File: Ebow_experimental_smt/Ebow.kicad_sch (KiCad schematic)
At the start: 9 parts, among them J1 Conn_01x02, U1 LM386

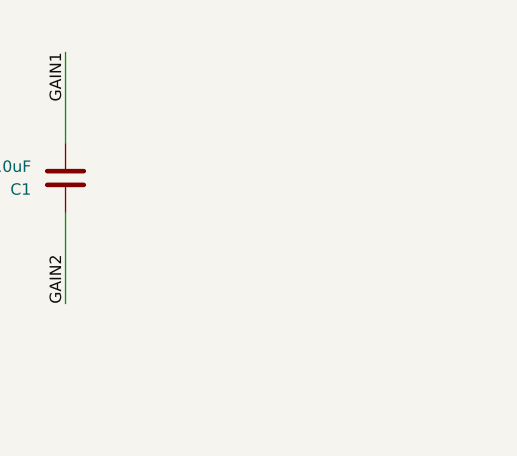
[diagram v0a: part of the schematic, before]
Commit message: Added smt version.
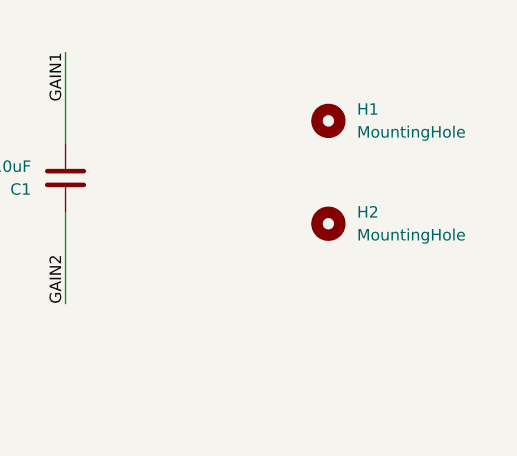
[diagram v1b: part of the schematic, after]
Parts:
- added H1, H2: MountingHole, MountingHole:MountingHole_2.5mm_Pad_TopBottom, symbol Mechanical:MountingHole
- C1, C2: footprint Capacitor_THT:CP_Radial_D5.0mm_P2.00mm -> Capacitor_SMD:C_Elec_4x5.8
- C3: footprint Capacitor_THT:C_Disc_D3.0mm_W2.0mm_P2.50mm -> Capacitor_SMD:C_0805_2012Metric_Pad1.18x1.45mm_HandSolder
- C4: footprint Capacitor_THT:CP_Radial_D8.0mm_P3.50mm -> Capacitor_SMD:CP_Elec_8x6.9
- L1, L2: footprint Buzzer_Beeper:Buzzer_D14mm_H7mm_P10mm -> Inductor_SMD:L_Taiyo-Yuden_NR-80xx_HandSoldering
- R1: footprint Resistor_THT:R_Axial_DIN0207_L6.3mm_D2.5mm_P15.24mm_Horizontal -> Resistor_SMD:R_0805_2012Metric_Pad1.20x1.40mm_HandSolder
- U1: footprint Package_DIP:DIP-8_W7.62mm_Socket -> Package_SO:SOIC-8_3.9x4.9mm_P1.27mm
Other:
- title: (none) -> Sustainer
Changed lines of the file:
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@@
 (kicad_sch (version 20211123) (generator eeschema)
   (paper "A4")
+  (title_block
+    (title "Sustainer")
+    (rev "A")
+  )
   (junction (at 127 145.415) (diameter 0) (color 0 0 0 0)
   )
@@
       (effects (font (size 1.27 1.27)) (justify right))
     )
-    (property "Footprint" "Capacitor_THT:C_Disc_D3.0mm_W2.0mm_P2.50mm" (id 2) (at 165.4048 127 0)
+    (property "Footprint" "Capacitor_SMD:C_0805_2012Metric_Pad1.18x1.45mm_HandSolder" (id 2) (at 165.4048 127 0)
       (effects (font (size 1.27 1.27)) hide)
     )
@@
       (effects (font (size 1.27 1.27)) (justify left))
     )
-    (property "Footprint" "Resistor_THT:R_Axial_DIN0207_L6.3mm_D2.5mm_P15.24mm_Horizontal" (id 2) (at 164.592 140.335 90)
+    (property "Footprint" "Resistor_SMD:R_0805_2012Metric_Pad1.20x1.40mm_HandSolder" (id 2) (at 164.592 140.335 90)
       (effects (font (size 1.27 1.27)) hide)
     )
@@
       (effects (font (size 1.27 1.27)) (justify left))
     )
-    (property "Footprint" "Buzzer_Beeper:Buzzer_D14mm_H7mm_P10mm" (id 2) (at 203.835 111.125 0)
-      (effects (font (size 1.27 1.27)) hide)
-    )
-    (property "Datasheet" "~" (id 3) (at 203.835 111.125 0)
+    (property "Footprint" "Inductor_SMD:L_Taiyo-Yuden_NR-80xx_HandSoldering" (id 2) (at 203.835 111.125 0)
+      (effects (font (size 1.27 1.27)) hide)
+    )
+    (property "Datasheet" "${KIPRJMOD}/datasheets/2108131830_SXN-Shun-Xiang-Nuo-Elec-SMNR6028-4R7MT_C266428.pdf" (id 3) (at 203.835 111.125 0)
       (effects (font (size 1.27 1.27)) hide)
     )
@@
       (effects (font (size 1.27 1.27)) (justify right))
     )
-    (property "Footprint" "Buzzer_Beeper:Buzzer_D14mm_H7mm_P10mm" (id 2) (at 89.535 108.585 0)
-      (effects (font (size 1.27 1.27)) hide)
-    )
-    (property "Datasheet" "~" (id 3) (at 89.535 108.585 0)
+    (property "Footprint" "Inductor_SMD:L_Taiyo-Yuden_NR-80xx_HandSoldering" (id 2) (at 89.535 108.585 0)
+      (effects (font (size 1.27 1.27)) hide)
+    )
+    (property "Datasheet" "${KIPRJMOD}/datasheets/2108131830_SXN-Shun-Xiang-Nuo-Elec-SMNR6028-4R7MT_C266428.pdf" (id 3) (at 89.535 108.585 0)
       (effects (font (size 1.27 1.27)) hide)
     )
@@
       (effects (font (size 1.27 1.27)) (justify right))
     )
-    (property "Footprint" "Capacitor_THT:CP_Radial_D5.0mm_P2.00mm" (id 2) (at 194.6402 35.56 0)
+    (property "Footprint" "Capacitor_SMD:C_Elec_4x5.8" (id 2) (at 194.6402 35.56 0)
       (effects (font (size 1.27 1.27)) hide)
     )
@@
       (effects (font (size 1.27 1.27)) (justify right))
     )
-    (property "Footprint" "Capacitor_THT:CP_Radial_D5.0mm_P2.00mm" (id 2) (at 163.4998 43.18 0)
+    (property "Footprint" "Capacitor_SMD:C_Elec_4x5.8" (id 2) (at 163.4998 43.18 0)
       (effects (font (size 1.27 1.27)) hide)
     )
@@
     (pin "1")
   )
+  (symbol (lib_id "Mechanical:MountingHole") (at 222.885 33.02 0) (unit 1)
+    (in_bom yes) (on_board yes) (fields_autoplaced)
+    (property "Reference" "H1" (id 0) (at 226.06 31.7499 0)
+      (effects (font (size 1.27 1.27)) (justify left))
+    )
+    (property "Value" "MountingHole" (id 1) (at 226.06 34.2899 0)
+      (effects (font (size 1.27 1.27)) (justify left))
+    )
+    (property "Footprint" "MountingHole:MountingHole_2.5mm_Pad_TopBottom" (id 2) (at 222.885 33.02 0)
+      (effects (font (size 1.27 1.27)) hide)
+    )
+    (property "Datasheet" "~" (id 3) (at 222.885 33.02 0)
+      (effects (font (size 1.27 1.27)) hide)
+    )
+  )
   (symbol (lib_id "power:+5V") (at 127 80.01 0) (unit 1)
     (in_bom yes) (on_board yes) (fields_autoplaced)
@@
     )
     (pin "1")
+  )
+  (symbol (lib_id "Mechanical:MountingHole") (at 222.885 44.45 0) (unit 1)
+    (in_bom yes) (on_board yes) (fields_autoplaced)
+    (property "Reference" "H2" (id 0) (at 226.06 43.1799 0)
+      (effects (font (size 1.27 1.27)) (justify left))
+    )
+    (property "Value" "MountingHole" (id 1) (at 226.06 45.7199 0)
+      (effects (font (size 1.27 1.27)) (justify left))
+    )
+    (property "Footprint" "MountingHole:MountingHole_2.5mm_Pad_TopBottom" (id 2) (at 222.885 44.45 0)
+      (effects (font (size 1.27 1.27)) hide)
+    )
+    (property "Datasheet" "~" (id 3) (at 222.885 44.45 0)
+      (effects (font (size 1.27 1.27)) hide)
+    )
   )
   (symbol (lib_id "Connector_Generic:Conn_01x02") (at 46.99 38.735 0) (mirror y) (unit 1)
@@
     (property "Reference" "C4" (id 0) (at 175.26 100.33 90))
     (property "Value" "220uF" (id 1) (at 175.26 102.87 90))
-    (property "Footprint" "Capacitor_THT:CP_Radial_D8.0mm_P3.50mm" (id 2) (at 179.07 106.3498 0)
+    (property "Footprint" "Capacitor_SMD:CP_Elec_8x6.9" (id 2) (at 179.07 106.3498 0)
       (effects (font (size 1.27 1.27)) hide)
     )
@@
     (property "Reference" "U1" (id 0) (at 139.7 102.616 0))
     (property "Value" "LM386" (id 1) (at 139.7 105.156 0))
-    (property "Footprint" "Package_DIP:DIP-8_W7.62mm_Socket" (id 2) (at 132.08 104.775 0)
-      (effects (font (size 1.27 1.27)) hide)
-    )
-    (property "Datasheet" "http://www.ti.com/lit/ds/symlink/lm386.pdf" (id 3) (at 134.62 102.235 0)
+    (property "Footprint" "Package_SO:SOIC-8_3.9x4.9mm_P1.27mm" (id 2) (at 132.08 104.775 0)
+      (effects (font (size 1.27 1.27)) hide)
+    )
+    (property "Datasheet" "${KIPRJMOD}/datasheets/lm386.pdf" (id 3) (at 134.62 102.235 0)
       (effects (font (size 1.27 1.27)) hide)
     )
@@
     )
     (path "/17c612b1-1712-43c4-bf42-da58958720f5"
-      (reference "C1") (unit 1) (value "10uF") (footprint "Capacitor_THT:CP_Radial_D5.0mm_P2.00mm")
+      (reference "C1") (unit 1) (value "10uF") (footprint "Capacitor_SMD:C_Elec_4x5.8")
     )
     (path "/1806c226-f868-413d-a730-b553d0b74cd3"
-      (reference "C2") (unit 1) (value "10uF") (footprint "Capacitor_THT:CP_Radial_D5.0mm_P2.00mm")
+      (reference "C2") (unit 1) (value "10uF") (footprint "Capacitor_SMD:C_Elec_4x5.8")
     )
     (path "/00fe35bc-98a8-4a57-8798-022f2f38780f"
-      (reference "C3") (unit 1) (value "47nF") (footprint "Capacitor_THT:C_Disc_D3.0mm_W2.0mm_P2.50mm")
+      (reference "C3") (unit 1) (value "47nF") (footprint "Capacitor_SMD:C_0805_2012Metric_Pad1.18x1.45mm_HandSolder")
     )
     (path "/95e2b8ef-b2ba-4938-97ca-cb0ef16712f6"
-      (reference "C4") (unit 1) (value "220uF") (footprint "Capacitor_THT:CP_Radial_D8.0mm_P3.50mm")
+      (reference "C4") (unit 1) (value "220uF") (footprint "Capacitor_SMD:CP_Elec_8x6.9")
+    )
+    (path "/310cf662-ee96-4e28-bf7a-f359466b8a24"
+      (reference "H1") (unit 1) (value "MountingHole") (footprint "MountingHole:MountingHole_2.5mm_Pad_TopBottom")
+    )
+    (path "/5ba09802-fc89-420d-9bc0-892b15911595"
+      (reference "H2") (unit 1) (value "MountingHole") (footprint "MountingHole:MountingHole_2.5mm_Pad_TopBottom")
     )
     (path "/86fa4628-2b3e-41e8-a65a-32e6da99fd1a"
@@
     )
     (path "/0fc6b024-f82b-4a82-bc84-87a221f28fe6"
-      (reference "L1") (unit 1) (value "L_Iron") (footprint "Buzzer_Beeper:Buzzer_D14mm_H7mm_P10mm")
+      (reference "L1") (unit 1) (value "L_Iron") (footprint "Inductor_SMD:L_Taiyo-Yuden_NR-80xx_HandSoldering")
     )
     (path "/0bff6920-0589-4a77-a48c-bd2c2345b946"
-      (reference "L2") (unit 1) (value "L_Iron") (footprint "Buzzer_Beeper:Buzzer_D14mm_H7mm_P10mm")
+      (reference "L2") (unit 1) (value "L_Iron") (footprint "Inductor_SMD:L_Taiyo-Yuden_NR-80xx_HandSoldering")
     )
     (path "/081ac558-1d49-471c-abf3-ed1a23f06285"
-      (reference "R1") (unit 1) (value "10R") (footprint "Resistor_THT:R_Axial_DIN0207_L6.3mm_D2.5mm_P15.24mm_Horizontal")
+      (reference "R1") (unit 1) (value "10R") (footprint "Resistor_SMD:R_0805_2012Metric_Pad1.20x1.40mm_HandSolder")
     )
     (path "/b3fe88ca-b472-4b17-9b69-956f1d81f7f1"
-      (reference "U1") (unit 1) (value "LM386") (footprint "Package_DIP:DIP-8_W7.62mm_Socket")
-    )
-  )
+      (reference "U1") (unit 1) (value "LM386") (footprint "Package_SO:SOIC-8_3.9x4.9mm_P1.27mm")
+    )
+  )

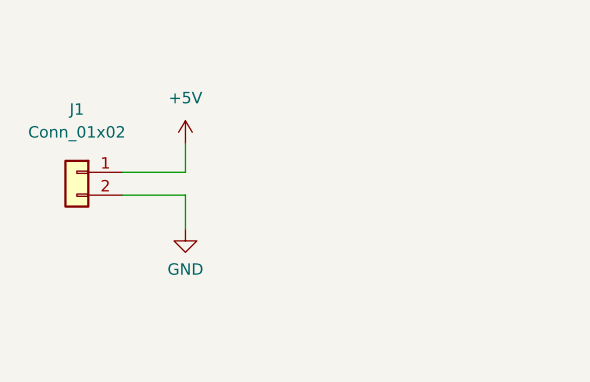
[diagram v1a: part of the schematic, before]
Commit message: updated schemas
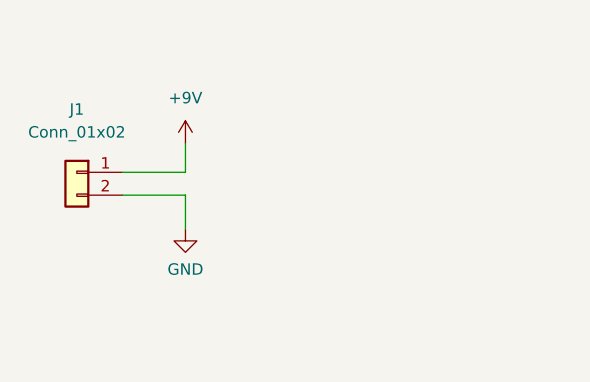
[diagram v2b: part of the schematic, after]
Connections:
- net +5V: no longer J1.1 (Pin_1)
- new net +9V: J1.1 (Pin_1)
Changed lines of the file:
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@@
     )
+  )
+  (symbol (lib_id "power:+9V") (at 59.055 35.56 0) (unit 1)
+    (in_bom yes) (on_board yes) (fields_autoplaced)
+    (property "Reference" "#PWR?" (id 0) (at 59.055 39.37 0)
+      (effects (font (size 1.27 1.27)) hide)
+    )
+    (property "Value" "+9V" (id 1) (at 59.055 30.48 0))
+    (property "Footprint" "" (id 2) (at 59.055 35.56 0)
+      (effects (font (size 1.27 1.27)) hide)
+    )
+    (property "Datasheet" "" (id 3) (at 59.055 35.56 0)
+      (effects (font (size 1.27 1.27)) hide)
+    )
+    (pin "1")
   )
   (symbol (lib_id "power:+5V") (at 127 80.01 0) (unit 1)
@@
     (pin "1")
   )
-  (symbol (lib_id "power:+5V") (at 59.055 35.56 0) (unit 1)
-    (in_bom yes) (on_board yes) (fields_autoplaced)
-    (property "Reference" "#PWR02" (id 0) (at 59.055 39.37 0)
-      (effects (font (size 1.27 1.27)) hide)
-    )
-    (property "Value" "+5V" (id 1) (at 59.055 30.48 0))
-    (property "Footprint" "" (id 2) (at 59.055 35.56 0)
-      (effects (font (size 1.27 1.27)) hide)
-    )
-    (property "Datasheet" "" (id 3) (at 59.055 35.56 0)
-      (effects (font (size 1.27 1.27)) hide)
-    )
-    (pin "1")
-  )
   (symbol (lib_id "Amplifier_Audio:LM386") (at 129.54 107.315 0) (unit 1)
     (in_bom yes) (on_board yes) (fields_autoplaced)
@@
       (reference "#PWR01") (unit 1) (value "GND") (footprint "")
     )
-    (path "/b14f207c-4c8e-4a7c-a74a-39cd24bc2d4c"
-      (reference "#PWR02") (unit 1) (value "+5V") (footprint "")
-    )
     (path "/92979cff-1e7c-4fc6-a0d2-82f65b7c20ae"
       (reference "#PWR03") (unit 1) (value "GND") (footprint "")
@@
       (reference "#PWR09") (unit 1) (value "GND") (footprint "")
     )
+    (path "/3e525ee9-d2a7-4d3c-a5be-81e97a45e5b0"
+      (reference "#PWR?") (unit 1) (value "+9V") (footprint "")
+    )
     (path "/17c612b1-1712-43c4-bf42-da58958720f5"

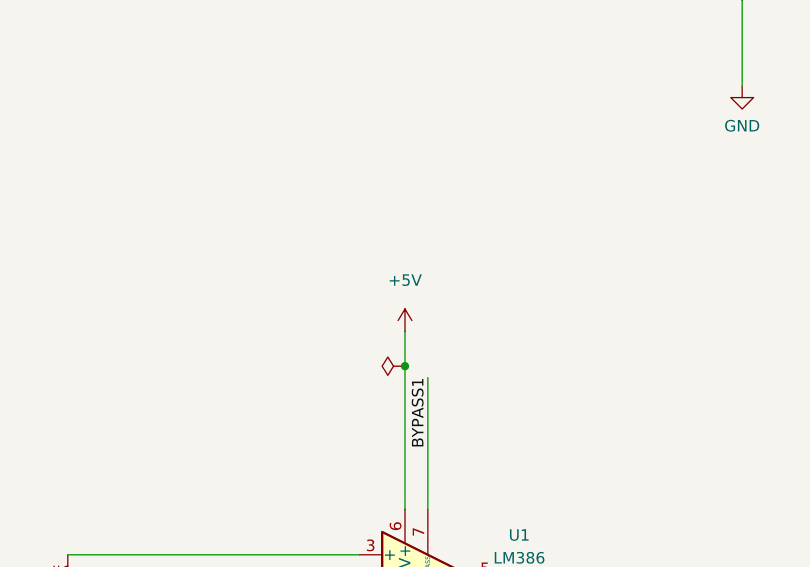
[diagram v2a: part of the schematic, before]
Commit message: updated power rail error
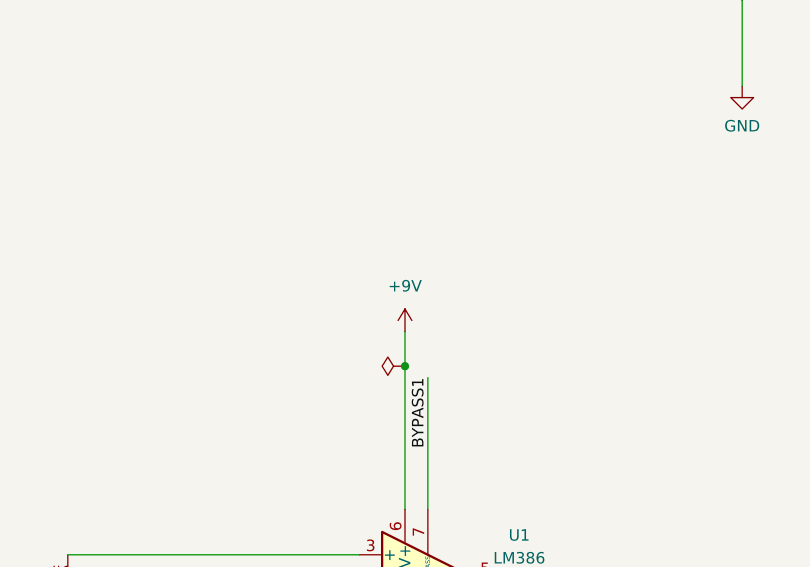
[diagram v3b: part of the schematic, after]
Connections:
- net +5V is gone; now on net +9V: U1.6 (V+)
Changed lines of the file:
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@@
     )
+  )
+  (symbol (lib_id "power:+9V") (at 127 80.01 0) (unit 1)
+    (in_bom yes) (on_board yes) (fields_autoplaced)
+    (property "Reference" "#PWR?" (id 0) (at 127 83.82 0)
+      (effects (font (size 1.27 1.27)) hide)
+    )
+    (property "Value" "+9V" (id 1) (at 127 74.93 0))
+    (property "Footprint" "" (id 2) (at 127 80.01 0)
+      (effects (font (size 1.27 1.27)) hide)
+    )
+    (property "Datasheet" "" (id 3) (at 127 80.01 0)
+      (effects (font (size 1.27 1.27)) hide)
+    )
+    (pin "1")
   )
   (symbol (lib_id "power:+9V") (at 59.055 35.56 0) (unit 1)
@@
     )
     (property "Datasheet" "" (id 3) (at 59.055 35.56 0)
-      (effects (font (size 1.27 1.27)) hide)
-    )
-    (pin "1")
-  )
-  (symbol (lib_id "power:+5V") (at 127 80.01 0) (unit 1)
-    (in_bom yes) (on_board yes) (fields_autoplaced)
-    (property "Reference" "#PWR04" (id 0) (at 127 83.82 0)
-      (effects (font (size 1.27 1.27)) hide)
-    )
-    (property "Value" "+5V" (id 1) (at 127 74.295 0))
-    (property "Footprint" "" (id 2) (at 127 80.01 0)
-      (effects (font (size 1.27 1.27)) hide)
-    )
-    (property "Datasheet" "" (id 3) (at 127 80.01 0)
       (effects (font (size 1.27 1.27)) hide)
     )
@@
       (reference "#PWR03") (unit 1) (value "GND") (footprint "")
     )
-    (path "/48b7a76d-e799-461e-8984-ba9b128240cc"
-      (reference "#PWR04") (unit 1) (value "+5V") (footprint "")
-    )
     (path "/1b7db835-fd9a-4ab9-9a0d-b6f1bc70ca53"
       (reference "#PWR05") (unit 1) (value "GND") (footprint "")
@@
       (reference "#PWR09") (unit 1) (value "GND") (footprint "")
     )
+    (path "/3b7b3371-59df-4376-9ad0-cdf5e021b5c1"
+      (reference "#PWR?") (unit 1) (value "+9V") (footprint "")
+    )
     (path "/3e525ee9-d2a7-4d3c-a5be-81e97a45e5b0"

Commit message: added inductor part number (SMNR6028-4R7MT)
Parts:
- L1, L2: value L_Iron -> SMNR6028-4R7MT
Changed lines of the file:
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@@
       (effects (font (size 1.27 1.27)) (justify left))
     )
-    (property "Value" "L_Iron" (id 1) (at 206.375 112.3949 0)
+    (property "Value" "SMNR6028-4R7MT" (id 1) (at 206.375 112.3949 0)
       (effects (font (size 1.27 1.27)) (justify left))
     )
@@
       (effects (font (size 1.27 1.27)) (justify right))
     )
-    (property "Value" "L_Iron" (id 1) (at 90.17 109.8549 0)
+    (property "Value" "SMNR6028-4R7MT" (id 1) (at 90.17 109.8549 0)
       (effects (font (size 1.27 1.27)) (justify right))
     )
@@
     )
     (path "/0fc6b024-f82b-4a82-bc84-87a221f28fe6"
-      (reference "L1") (unit 1) (value "L_Iron") (footprint "Inductor_SMD:L_Taiyo-Yuden_NR-80xx_HandSoldering")
+      (reference "L1") (unit 1) (value "SMNR6028-4R7MT") (footprint "Inductor_SMD:L_Taiyo-Yuden_NR-80xx_HandSoldering")
     )
     (path "/0bff6920-0589-4a77-a48c-bd2c2345b946"
-      (reference "L2") (unit 1) (value "L_Iron") (footprint "Inductor_SMD:L_Taiyo-Yuden_NR-80xx_HandSoldering")
+      (reference "L2") (unit 1) (value "SMNR6028-4R7MT") (footprint "Inductor_SMD:L_Taiyo-Yuden_NR-80xx_HandSoldering")
     )
     (path "/081ac558-1d49-471c-abf3-ed1a23f06285"
